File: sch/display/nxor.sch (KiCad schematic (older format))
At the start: 14 parts, among them Q1 2N7002, Q2 2N7002, Q3 2N7002, Q4 2N7002

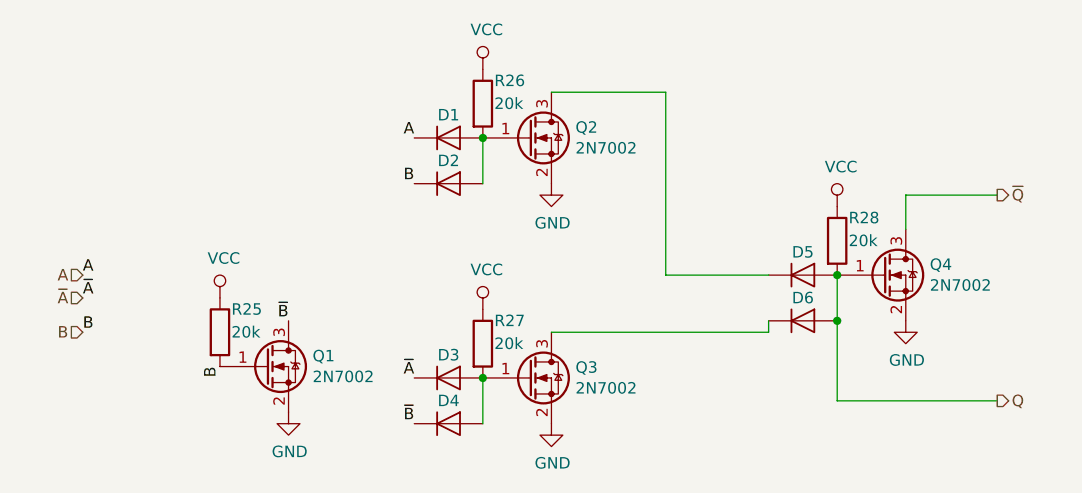
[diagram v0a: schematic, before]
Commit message: 7-segment indicator footprint is added
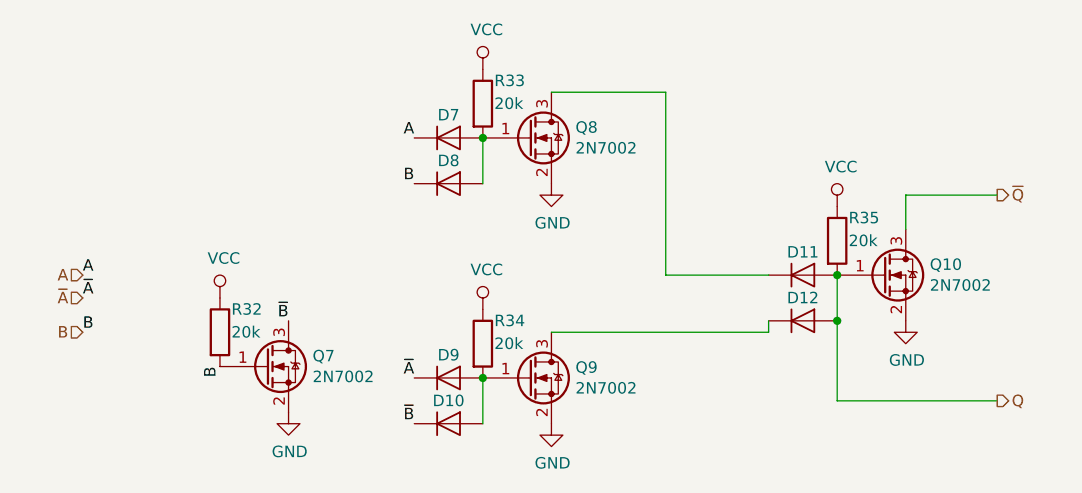
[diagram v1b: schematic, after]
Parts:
- D1, D2, D3, D4, D5, D6: footprint (none) -> Diode_SMD:D_MiniMELF
- Q3: renamed from Q1; footprint (none) -> Package_TO_SOT_SMD:SOT-23
- Q4: renamed from Q2; footprint (none) -> Package_TO_SOT_SMD:SOT-23
- Q5: renamed from Q3; footprint (none) -> Package_TO_SOT_SMD:SOT-23
- Q6: renamed from Q4; footprint (none) -> Package_TO_SOT_SMD:SOT-23
- R28: renamed from R25; footprint (none) -> Resistor_SMD:R_0805_2012Metric
- R29: renamed from R26; footprint (none) -> Resistor_SMD:R_0805_2012Metric
- R30: renamed from R27; footprint (none) -> Resistor_SMD:R_0805_2012Metric
- R31: renamed from R28; footprint (none) -> Resistor_SMD:R_0805_2012Metric

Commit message: Added datasheets, set component values, calculated LED resistors
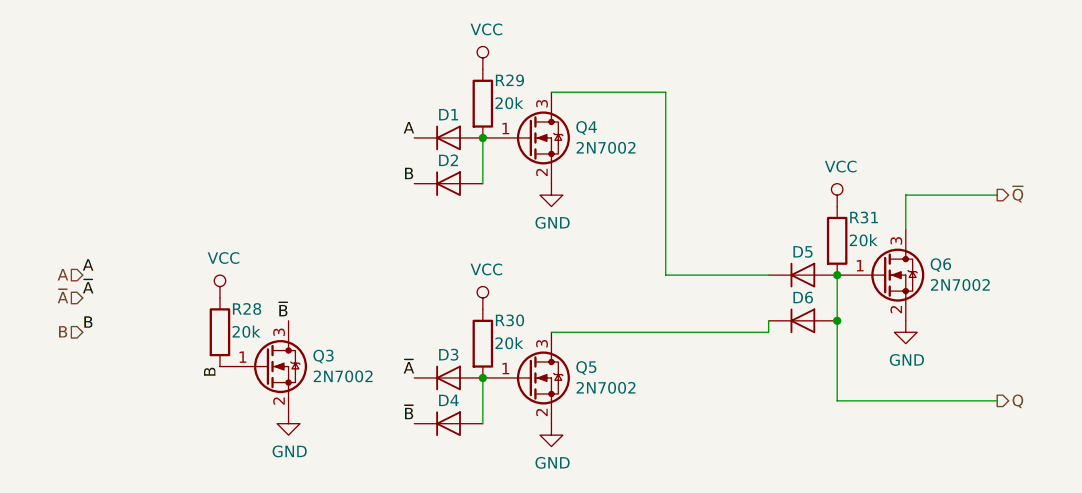
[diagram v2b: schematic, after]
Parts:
- D1, D2, D3, D4, D5, D6: value D -> LL103C
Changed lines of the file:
@@
 AR Path="/5C134276/5C135129" Ref="D3"  Part="1"
 AR Path="/5C14209F/5C135129" Ref="D9"  Part="1"
-F 0 "D9" H 3500 2800 50  0000 C CNN
-F 1 "D" H 3500 2825 50  0001 C CNN
+F 0 "D3" H 3500 2800 50  0000 C CNN
+F 1 "LL103C" H 3500 2825 50  0001 C CNN
 F 2 "Diode_SMD:D_MiniMELF" H 3500 2700 50  0001 C CNN
 F 3 "~" H 3500 2700 50  0001 C CNN
@@
 AR Path="/5C134276/5C1355E3" Ref="Q5"  Part="1"
 AR Path="/5C14209F/5C1355E3" Ref="Q9"  Part="1"
-F 0 "Q9" H 4055 2746 50  0000 L CNN
+F 0 "Q5" H 4055 2746 50  0000 L CNN
 F 1 "2N7002" H 4055 2655 50  0000 L CNN
 F 2 "Package_TO_SOT_SMD:SOT-23" H 4050 2800 50  0001 C CNN
@@
 AR Path="/5C134276/5C13AD9F" Ref="R30"  Part="1"
 AR Path="/5C14209F/5C13AD9F" Ref="R34"  Part="1"
-F 0 "R34" H 3700 2650 50  0000 L CNN
+F 0 "R30" H 3700 2650 50  0000 L CNN
 F 1 "20k" H 3700 2550 50  0000 L CNN
 F 2 "Resistor_SMD:R_0805_2012Metric" V 3580 2550 50  0001 C CNN
@@
 AR Path="/5C134276/5C13AEE3" Ref="#PWR022"  Part="1"
 AR Path="/5C14209F/5C13AEE3" Ref="#PWR030"  Part="1"
-F 0 "#PWR030" H 3650 2250 50  0001 C CNN
+F 0 "#PWR022" H 3650 2250 50  0001 C CNN
 F 1 "VCC" H 3667 2573 50  0000 C CNN
 F 2 "" H 3650 2400 50  0001 C CNN
@@
 AR Path="/5C134276/5C13AF57" Ref="#PWR024"  Part="1"
 AR Path="/5C14209F/5C13AF57" Ref="#PWR032"  Part="1"
-F 0 "#PWR032" H 3950 2650 50  0001 C CNN
+F 0 "#PWR024" H 3950 2650 50  0001 C CNN
 F 1 "GND" H 3955 2727 50  0000 C CNN
 F 2 "" H 3950 2900 50  0001 C CNN
@@
 AR Path="/5C134276/5C13AF6F" Ref="D4"  Part="1"
 AR Path="/5C14209F/5C13AF6F" Ref="D10"  Part="1"
-F 0 "D10" H 3500 3000 50  0000 C CNN
-F 1 "D" H 3500 3025 50  0001 C CNN
+F 0 "D4" H 3500 3000 50  0000 C CNN
+F 1 "LL103C" H 3500 3025 50  0001 C CNN
 F 2 "Diode_SMD:D_MiniMELF" H 3500 2900 50  0001 C CNN
 F 3 "~" H 3500 2900 50  0001 C CNN
@@
 AR Path="/5C134276/5C13B0A5" Ref="D1"  Part="1"
 AR Path="/5C14209F/5C13B0A5" Ref="D7"  Part="1"
-F 0 "D7" H 3500 1750 50  0000 C CNN
-F 1 "D" H 3500 1775 50  0001 C CNN
+F 0 "D1" H 3500 1750 50  0000 C CNN
+F 1 "LL103C" H 3500 1775 50  0001 C CNN
 F 2 "Diode_SMD:D_MiniMELF" H 3500 1650 50  0001 C CNN
 F 3 "~" H 3500 1650 50  0001 C CNN
@@
 AR Path="/5C134276/5C13B0AC" Ref="Q4"  Part="1"
 AR Path="/5C14209F/5C13B0AC" Ref="Q8"  Part="1"
-F 0 "Q8" H 4055 1696 50  0000 L CNN
+F 0 "Q4" H 4055 1696 50  0000 L CNN
 F 1 "2N7002" H 4055 1605 50  0000 L CNN
 F 2 "Package_TO_SOT_SMD:SOT-23" H 4050 1750 50  0001 C CNN
@@
 AR Path="/5C134276/5C13B0B3" Ref="R29"  Part="1"
 AR Path="/5C14209F/5C13B0B3" Ref="R33"  Part="1"
-F 0 "R33" H 3700 1600 50  0000 L CNN
+F 0 "R29" H 3700 1600 50  0000 L CNN
 F 1 "20k" H 3700 1500 50  0000 L CNN
 F 2 "Resistor_SMD:R_0805_2012Metric" V 3580 1500 50  0001 C CNN
@@
 AR Path="/5C134276/5C13B0BB" Ref="#PWR021"  Part="1"
 AR Path="/5C14209F/5C13B0BB" Ref="#PWR029"  Part="1"
-F 0 "#PWR029" H 3650 1200 50  0001 C CNN
+F 0 "#PWR021" H 3650 1200 50  0001 C CNN
 F 1 "VCC" H 3667 1523 50  0000 C CNN
 F 2 "" H 3650 1350 50  0001 C CNN
@@
 AR Path="/5C134276/5C13B0C1" Ref="#PWR023"  Part="1"
 AR Path="/5C14209F/5C13B0C1" Ref="#PWR031"  Part="1"
-F 0 "#PWR031" H 3950 1600 50  0001 C CNN
+F 0 "#PWR023" H 3950 1600 50  0001 C CNN
 F 1 "GND" H 3955 1677 50  0000 C CNN
 F 2 "" H 3950 1850 50  0001 C CNN
@@
 AR Path="/5C134276/5C13B0C7" Ref="D2"  Part="1"
 AR Path="/5C14209F/5C13B0C7" Ref="D8"  Part="1"
-F 0 "D8" H 3500 1950 50  0000 C CNN
-F 1 "D" H 3500 1975 50  0001 C CNN
+F 0 "D2" H 3500 1950 50  0000 C CNN
+F 1 "LL103C" H 3500 1975 50  0001 C CNN
 F 2 "Diode_SMD:D_MiniMELF" H 3500 1850 50  0001 C CNN
 F 3 "~" H 3500 1850 50  0001 C CNN
@@
 AR Path="/5C134276/5C13B135" Ref="D5"  Part="1"
 AR Path="/5C14209F/5C13B135" Ref="D11"  Part="1"
-F 0 "D11" H 5050 2350 50  0000 C CNN
-F 1 "D" H 5050 2375 50  0001 C CNN
+F 0 "D5" H 5050 2350 50  0000 C CNN
+F 1 "LL103C" H 5050 2375 50  0001 C CNN
 F 2 "Diode_SMD:D_MiniMELF" H 5050 2250 50  0001 C CNN
 F 3 "~" H 5050 2250 50  0001 C CNN
@@
 AR Path="/5C134276/5C13B13C" Ref="Q6"  Part="1"
 AR Path="/5C14209F/5C13B13C" Ref="Q10"  Part="1"
-F 0 "Q10" H 5605 2296 50  0000 L CNN
+F 0 "Q6" H 5605 2296 50  0000 L CNN
 F 1 "2N7002" H 5605 2205 50  0000 L CNN
 F 2 "Package_TO_SOT_SMD:SOT-23" H 5600 2350 50  0001 C CNN
@@
 AR Path="/5C134276/5C13B143" Ref="R31"  Part="1"
 AR Path="/5C14209F/5C13B143" Ref="R35"  Part="1"
-F 0 "R35" H 5250 2200 50  0000 L CNN
+F 0 "R31" H 5250 2200 50  0000 L CNN
 F 1 "20k" H 5250 2100 50  0000 L CNN
 F 2 "Resistor_SMD:R_0805_2012Metric" V 5130 2100 50  0001 C CNN
@@
 AR Path="/5C134276/5C13B14B" Ref="#PWR025"  Part="1"
 AR Path="/5C14209F/5C13B14B" Ref="#PWR033"  Part="1"
-F 0 "#PWR033" H 5200 1800 50  0001 C CNN
+F 0 "#PWR025" H 5200 1800 50  0001 C CNN
 F 1 "VCC" H 5217 2123 50  0000 C CNN
 F 2 "" H 5200 1950 50  0001 C CNN
@@
 AR Path="/5C134276/5C13B151" Ref="#PWR026"  Part="1"
 AR Path="/5C14209F/5C13B151" Ref="#PWR034"  Part="1"
-F 0 "#PWR034" H 5500 2200 50  0001 C CNN
+F 0 "#PWR026" H 5500 2200 50  0001 C CNN
 F 1 "GND" H 5505 2277 50  0000 C CNN
 F 2 "" H 5500 2450 50  0001 C CNN
@@
 AR Path="/5C134276/5C13B157" Ref="D6"  Part="1"
 AR Path="/5C14209F/5C13B157" Ref="D12"  Part="1"
-F 0 "D12" H 5050 2550 50  0000 C CNN
-F 1 "D" H 5050 2575 50  0001 C CNN
+F 0 "D6" H 5050 2550 50  0000 C CNN
+F 1 "LL103C" H 5050 2575 50  0001 C CNN
 F 2 "Diode_SMD:D_MiniMELF" H 5050 2450 50  0001 C CNN
 F 3 "~" H 5050 2450 50  0001 C CNN
@@
 AR Path="/5C134276/5C13B177" Ref="Q3"  Part="1"
 AR Path="/5C14209F/5C13B177" Ref="Q7"  Part="1"
-F 0 "Q7" H 2905 2696 50  0000 L CNN
+F 0 "Q3" H 2905 2696 50  0000 L CNN
 F 1 "2N7002" H 2905 2605 50  0000 L CNN
 F 2 "Package_TO_SOT_SMD:SOT-23" H 2900 2750 50  0001 C CNN
@@
 AR Path="/5C134276/5C13B362" Ref="#PWR020"  Part="1"
 AR Path="/5C14209F/5C13B362" Ref="#PWR028"  Part="1"
-F 0 "#PWR028" H 2800 2600 50  0001 C CNN
+F 0 "#PWR020" H 2800 2600 50  0001 C CNN
 F 1 "GND" H 2805 2677 50  0000 C CNN
 F 2 "" H 2800 2850 50  0001 C CNN
@@
 AR Path="/5C134276/5C13B3BC" Ref="R28"  Part="1"
 AR Path="/5C14209F/5C13B3BC" Ref="R32"  Part="1"
-F 0 "R32" H 2550 2600 50  0000 L CNN
+F 0 "R28" H 2550 2600 50  0000 L CNN
 F 1 "20k" H 2550 2500 50  0000 L CNN
 F 2 "Resistor_SMD:R_0805_2012Metric" V 2430 2500 50  0001 C CNN
@@
 AR Path="/5C134276/5C13B3F8" Ref="#PWR019"  Part="1"
 AR Path="/5C14209F/5C13B3F8" Ref="#PWR027"  Part="1"
-F 0 "#PWR027" H 2500 2200 50  0001 C CNN
+F 0 "#PWR019" H 2500 2200 50  0001 C CNN
 F 1 "VCC" H 2517 2523 50  0000 C CNN
 F 2 "" H 2500 2350 50  0001 C CNN

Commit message: Display board, BOM updated
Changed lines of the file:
@@
 $Descr A4 11693 8268
 encoding utf-8
-Sheet 3 4
+Sheet 3 3
 Title ""
 Date ""
@@
 AR Path="/5C134276/5C135129" Ref="D3"  Part="1"
 AR Path="/5C14209F/5C135129" Ref="D9"  Part="1"
-F 0 "D3" H 3500 2800 50  0000 C CNN
+F 0 "D9" H 3500 2800 50  0000 C CNN
 F 1 "LL103C" H 3500 2825 50  0001 C CNN
 F 2 "Diode_SMD:D_MiniMELF" H 3500 2700 50  0001 C CNN
@@
 AR Path="/5C134276/5C1355E3" Ref="Q5"  Part="1"
 AR Path="/5C14209F/5C1355E3" Ref="Q9"  Part="1"
-F 0 "Q5" H 4055 2746 50  0000 L CNN
+F 0 "Q9" H 4055 2746 50  0000 L CNN
 F 1 "2N7002" H 4055 2655 50  0000 L CNN
 F 2 "Package_TO_SOT_SMD:SOT-23" H 4050 2800 50  0001 C CNN
@@
 AR Path="/5C134276/5C13AD9F" Ref="R30"  Part="1"
 AR Path="/5C14209F/5C13AD9F" Ref="R34"  Part="1"
-F 0 "R30" H 3700 2650 50  0000 L CNN
+F 0 "R34" H 3700 2650 50  0000 L CNN
 F 1 "20k" H 3700 2550 50  0000 L CNN
 F 2 "Resistor_SMD:R_0805_2012Metric" V 3580 2550 50  0001 C CNN
@@
 AR Path="/5C134276/5C13AEE3" Ref="#PWR022"  Part="1"
 AR Path="/5C14209F/5C13AEE3" Ref="#PWR030"  Part="1"
-F 0 "#PWR022" H 3650 2250 50  0001 C CNN
+F 0 "#PWR030" H 3650 2250 50  0001 C CNN
 F 1 "VCC" H 3667 2573 50  0000 C CNN
 F 2 "" H 3650 2400 50  0001 C CNN
@@
 AR Path="/5C134276/5C13AF57" Ref="#PWR024"  Part="1"
 AR Path="/5C14209F/5C13AF57" Ref="#PWR032"  Part="1"
-F 0 "#PWR024" H 3950 2650 50  0001 C CNN
+F 0 "#PWR032" H 3950 2650 50  0001 C CNN
 F 1 "GND" H 3955 2727 50  0000 C CNN
 F 2 "" H 3950 2900 50  0001 C CNN
@@
 AR Path="/5C134276/5C13AF6F" Ref="D4"  Part="1"
 AR Path="/5C14209F/5C13AF6F" Ref="D10"  Part="1"
-F 0 "D4" H 3500 3000 50  0000 C CNN
+F 0 "D10" H 3500 3000 50  0000 C CNN
 F 1 "LL103C" H 3500 3025 50  0001 C CNN
 F 2 "Diode_SMD:D_MiniMELF" H 3500 2900 50  0001 C CNN
@@
 AR Path="/5C134276/5C13B0A5" Ref="D1"  Part="1"
 AR Path="/5C14209F/5C13B0A5" Ref="D7"  Part="1"
-F 0 "D1" H 3500 1750 50  0000 C CNN
+F 0 "D7" H 3500 1750 50  0000 C CNN
 F 1 "LL103C" H 3500 1775 50  0001 C CNN
 F 2 "Diode_SMD:D_MiniMELF" H 3500 1650 50  0001 C CNN
@@
 AR Path="/5C134276/5C13B0AC" Ref="Q4"  Part="1"
 AR Path="/5C14209F/5C13B0AC" Ref="Q8"  Part="1"
-F 0 "Q4" H 4055 1696 50  0000 L CNN
+F 0 "Q8" H 4055 1696 50  0000 L CNN
 F 1 "2N7002" H 4055 1605 50  0000 L CNN
 F 2 "Package_TO_SOT_SMD:SOT-23" H 4050 1750 50  0001 C CNN
@@
 AR Path="/5C134276/5C13B0B3" Ref="R29"  Part="1"
 AR Path="/5C14209F/5C13B0B3" Ref="R33"  Part="1"
-F 0 "R29" H 3700 1600 50  0000 L CNN
+F 0 "R33" H 3700 1600 50  0000 L CNN
 F 1 "20k" H 3700 1500 50  0000 L CNN
 F 2 "Resistor_SMD:R_0805_2012Metric" V 3580 1500 50  0001 C CNN
@@
 AR Path="/5C134276/5C13B0BB" Ref="#PWR021"  Part="1"
 AR Path="/5C14209F/5C13B0BB" Ref="#PWR029"  Part="1"
-F 0 "#PWR021" H 3650 1200 50  0001 C CNN
+F 0 "#PWR029" H 3650 1200 50  0001 C CNN
 F 1 "VCC" H 3667 1523 50  0000 C CNN
 F 2 "" H 3650 1350 50  0001 C CNN
@@
 AR Path="/5C134276/5C13B0C1" Ref="#PWR023"  Part="1"
 AR Path="/5C14209F/5C13B0C1" Ref="#PWR031"  Part="1"
-F 0 "#PWR023" H 3950 1600 50  0001 C CNN
+F 0 "#PWR031" H 3950 1600 50  0001 C CNN
 F 1 "GND" H 3955 1677 50  0000 C CNN
 F 2 "" H 3950 1850 50  0001 C CNN
@@
 AR Path="/5C134276/5C13B0C7" Ref="D2"  Part="1"
 AR Path="/5C14209F/5C13B0C7" Ref="D8"  Part="1"
-F 0 "D2" H 3500 1950 50  0000 C CNN
+F 0 "D8" H 3500 1950 50  0000 C CNN
 F 1 "LL103C" H 3500 1975 50  0001 C CNN
 F 2 "Diode_SMD:D_MiniMELF" H 3500 1850 50  0001 C CNN
@@
 AR Path="/5C134276/5C13B135" Ref="D5"  Part="1"
 AR Path="/5C14209F/5C13B135" Ref="D11"  Part="1"
-F 0 "D5" H 5050 2350 50  0000 C CNN
+F 0 "D11" H 5050 2350 50  0000 C CNN
 F 1 "LL103C" H 5050 2375 50  0001 C CNN
 F 2 "Diode_SMD:D_MiniMELF" H 5050 2250 50  0001 C CNN
@@
 AR Path="/5C134276/5C13B13C" Ref="Q6"  Part="1"
 AR Path="/5C14209F/5C13B13C" Ref="Q10"  Part="1"
-F 0 "Q6" H 5605 2296 50  0000 L CNN
+F 0 "Q10" H 5605 2296 50  0000 L CNN
 F 1 "2N7002" H 5605 2205 50  0000 L CNN
 F 2 "Package_TO_SOT_SMD:SOT-23" H 5600 2350 50  0001 C CNN
@@
 AR Path="/5C134276/5C13B143" Ref="R31"  Part="1"
 AR Path="/5C14209F/5C13B143" Ref="R35"  Part="1"
-F 0 "R31" H 5250 2200 50  0000 L CNN
+F 0 "R35" H 5250 2200 50  0000 L CNN
 F 1 "20k" H 5250 2100 50  0000 L CNN
 F 2 "Resistor_SMD:R_0805_2012Metric" V 5130 2100 50  0001 C CNN
@@
 AR Path="/5C134276/5C13B14B" Ref="#PWR025"  Part="1"
 AR Path="/5C14209F/5C13B14B" Ref="#PWR033"  Part="1"
-F 0 "#PWR025" H 5200 1800 50  0001 C CNN
+F 0 "#PWR033" H 5200 1800 50  0001 C CNN
 F 1 "VCC" H 5217 2123 50  0000 C CNN
 F 2 "" H 5200 1950 50  0001 C CNN
@@
 AR Path="/5C134276/5C13B151" Ref="#PWR026"  Part="1"
 AR Path="/5C14209F/5C13B151" Ref="#PWR034"  Part="1"
-F 0 "#PWR026" H 5500 2200 50  0001 C CNN
+F 0 "#PWR034" H 5500 2200 50  0001 C CNN
 F 1 "GND" H 5505 2277 50  0000 C CNN
 F 2 "" H 5500 2450 50  0001 C CNN
@@
 AR Path="/5C134276/5C13B157" Ref="D6"  Part="1"
 AR Path="/5C14209F/5C13B157" Ref="D12"  Part="1"
-F 0 "D6" H 5050 2550 50  0000 C CNN
+F 0 "D12" H 5050 2550 50  0000 C CNN
 F 1 "LL103C" H 5050 2575 50  0001 C CNN
 F 2 "Diode_SMD:D_MiniMELF" H 5050 2450 50  0001 C CNN
@@
 AR Path="/5C134276/5C13B177" Ref="Q3"  Part="1"
 AR Path="/5C14209F/5C13B177" Ref="Q7"  Part="1"
-F 0 "Q3" H 2905 2696 50  0000 L CNN
+F 0 "Q7" H 2905 2696 50  0000 L CNN
 F 1 "2N7002" H 2905 2605 50  0000 L CNN
 F 2 "Package_TO_SOT_SMD:SOT-23" H 2900 2750 50  0001 C CNN
@@
 AR Path="/5C134276/5C13B362" Ref="#PWR020"  Part="1"
 AR Path="/5C14209F/5C13B362" Ref="#PWR028"  Part="1"
-F 0 "#PWR020" H 2800 2600 50  0001 C CNN
+F 0 "#PWR028" H 2800 2600 50  0001 C CNN
 F 1 "GND" H 2805 2677 50  0000 C CNN
 F 2 "" H 2800 2850 50  0001 C CNN
@@
 AR Path="/5C134276/5C13B3BC" Ref="R28"  Part="1"
 AR Path="/5C14209F/5C13B3BC" Ref="R32"  Part="1"
-F 0 "R28" H 2550 2600 50  0000 L CNN
+F 0 "R32" H 2550 2600 50  0000 L CNN
 F 1 "20k" H 2550 2500 50  0000 L CNN
 F 2 "Resistor_SMD:R_0805_2012Metric" V 2430 2500 50  0001 C CNN
@@
 AR Path="/5C134276/5C13B3F8" Ref="#PWR019"  Part="1"
 AR Path="/5C14209F/5C13B3F8" Ref="#PWR027"  Part="1"
-F 0 "#PWR019" H 2500 2200 50  0001 C CNN
+F 0 "#PWR027" H 2500 2200 50  0001 C CNN
 F 1 "VCC" H 2517 2523 50  0000 C CNN
 F 2 "" H 2500 2350 50  0001 C CNN
